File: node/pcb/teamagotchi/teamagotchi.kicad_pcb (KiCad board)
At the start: 2 copper layers, 75 x 112 mm, 24 parts, among them M1 Motor_DC, Q1 BC547, SW1 SW_Push, SW2 SW_Push, SW3 SW_Push, SW4 SW_Push, SW5 SW_Push, U1 3406

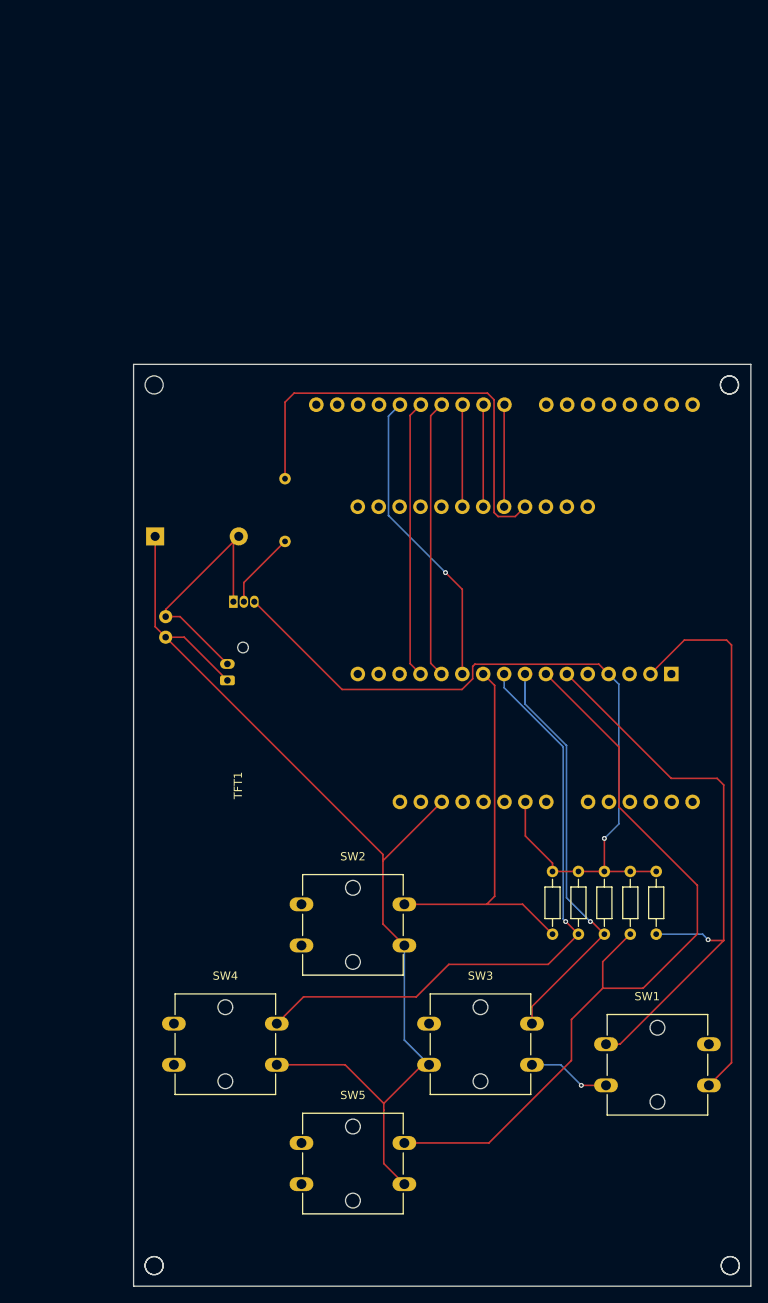
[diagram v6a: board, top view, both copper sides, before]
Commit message: added GND copper filling, added RIOT and HAW Logo
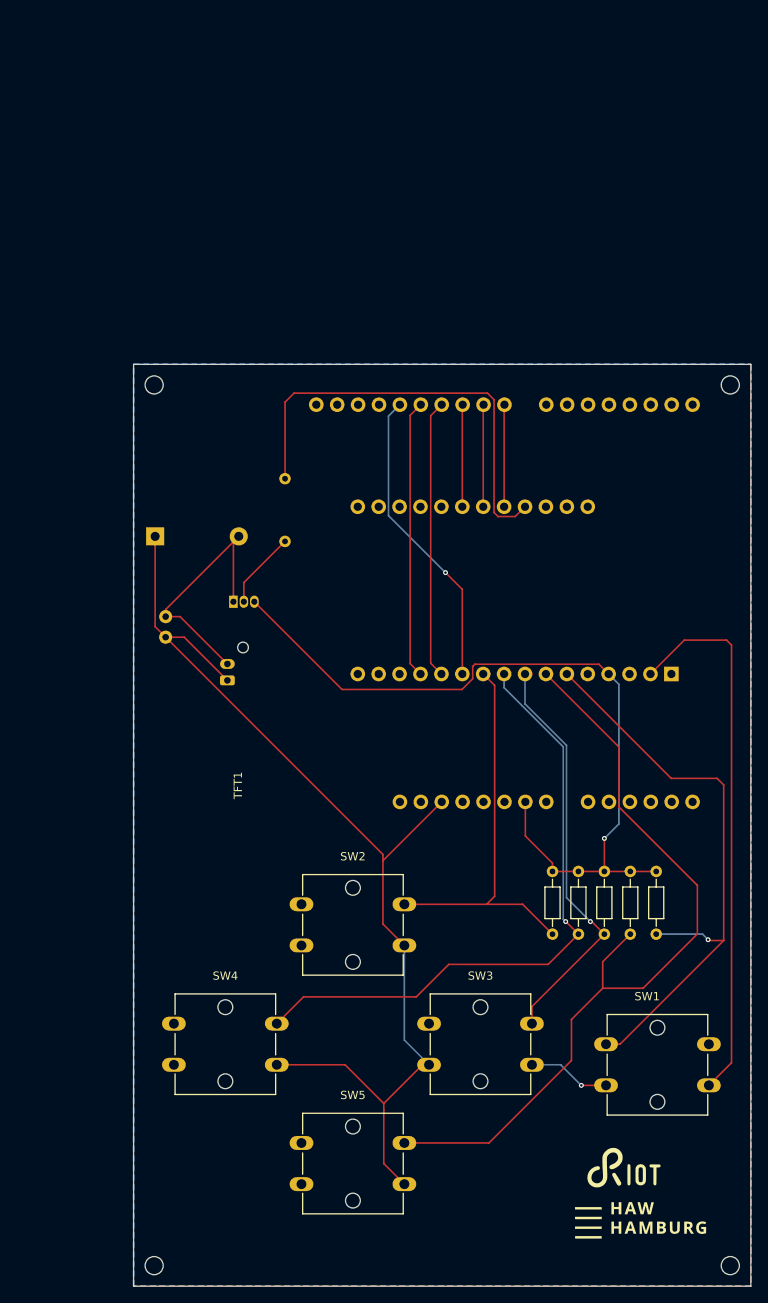
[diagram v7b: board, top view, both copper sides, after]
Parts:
- removed ? (x3): , 
- added G***: LOGO, Library:haw_logo_logo, F.Cu at (171.0, 150.7)
- added G***: LOGO, Library:riot_logo, F.Cu at (169.6, 144.3)
- moved REF** 0.10 mm to (182.5, 49.2)
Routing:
- added copper zone on B.Cu, net Net-(D1-K)
- added copper zone on F.Cu, net Net-(D1-K)

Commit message: added debouncing, some beautyfications
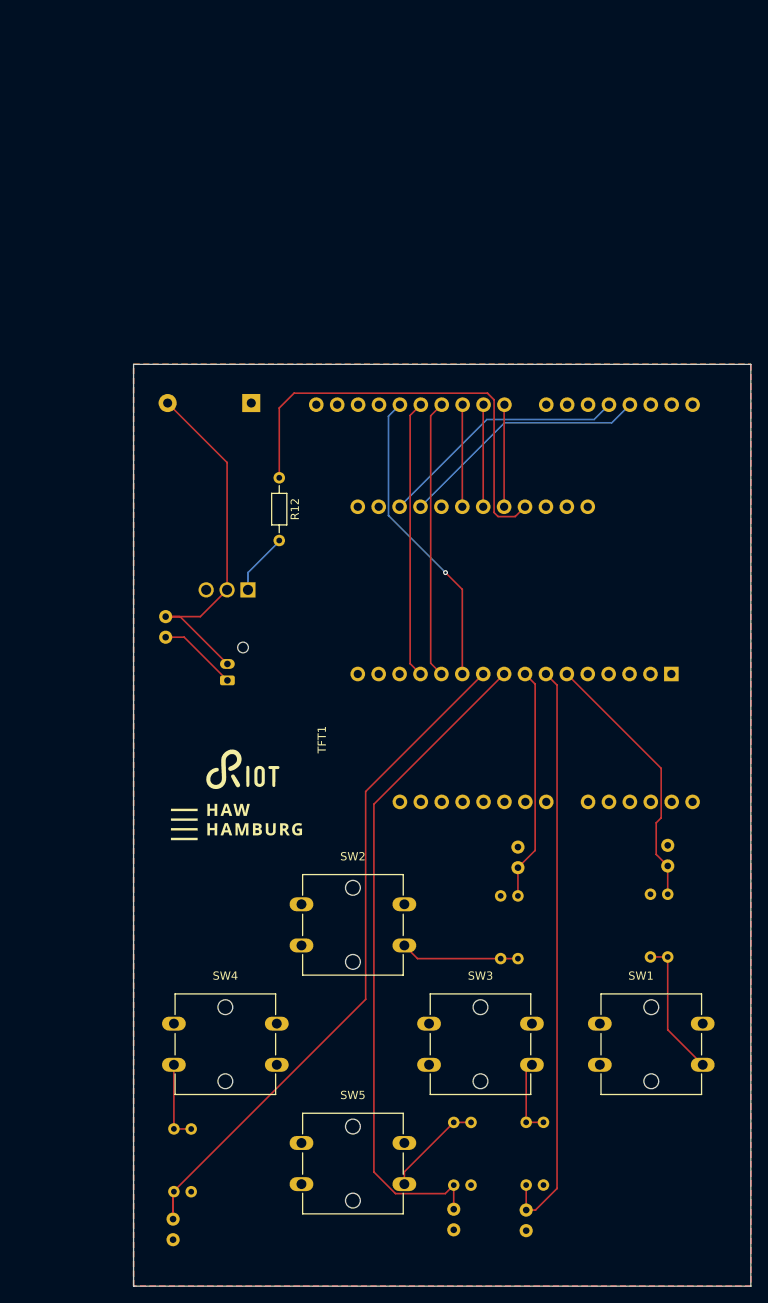
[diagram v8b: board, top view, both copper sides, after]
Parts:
- removed Q1: BC547, Package_TO_SOT_THT:TO-92_Inline
- removed REF** (x4): 2.2mm_M2, MountingHole:MountingHole_2.2mm_M2
- added C2: C, Capacitor_THT:C_Disc_D3.0mm_W1.6mm_P2.50mm, B.Cu at (174.9, 107.6)
- added C3: C, Capacitor_THT:C_Disc_D3.0mm_W1.6mm_P2.50mm, B.Cu at (156.7, 107.9)
- added C4: C, Capacitor_THT:C_Disc_D3.0mm_W1.6mm_P2.50mm, B.Cu at (157.7, 149.5)
- added C5: C, Capacitor_THT:C_Disc_D3.0mm_W1.6mm_P2.50mm, B.Cu at (114.8, 150.6)
- added C6: C, Capacitor_THT:C_Disc_D3.0mm_W1.6mm_P2.50mm, B.Cu at (148.9, 149.4)
- added Q2: IRLZ44N, Library:IRLZ44N, B.Cu at (121.3, 73.2)
- added R10: R, Resistor_THT:R_Axial_DIN0204_L3.6mm_D1.6mm_P7.62mm_Horizontal, B.Cu at (151.0, 146.4)
- added R12: R, Resistor_THT:R_Axial_DIN0204_L3.6mm_D1.6mm_P7.62mm_Horizontal, F.Cu at (127.7, 60.5)
- added R7: R, Resistor_THT:R_Axial_DIN0204_L3.6mm_D1.6mm_P7.62mm_Horizontal, B.Cu at (114.9, 147.2)
- added R8: R, Resistor_THT:R_Axial_DIN0204_L3.6mm_D1.6mm_P7.62mm_Horizontal, B.Cu at (117.0, 147.2)
- added R9: R, Resistor_THT:R_Axial_DIN0204_L3.6mm_D1.6mm_P7.62mm_Horizontal, B.Cu at (148.9, 146.4)
- R1, R2, R3, R4, R5: moved to B.Cu
- moved R6 91.4 mm to (159.8, 146.4), turned to 90 degrees
- moved G*** 68.9 mm to (121.9, 102.3)
- moved G*** 67.0 mm to (123.3, 95.9)
- moved R5 38.2 mm to (157.7, 146.4), turned to 90 degrees
- moved D1 20.0 mm to (124.3, 51.4), turned to 180 degrees
- moved R3 10.9 mm to (156.7, 111.3)
- moved R4 9.91 mm to (154.6, 111.3)
- moved R2 3.70 mm to (172.8, 111.1)
- moved R1 3.10 mm to (174.9, 111.1)
- moved SW1 2.61 mm to (166.6, 126.8)
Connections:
- net Net-(TFT1-D10/TFT_CS) renamed /TFT_CS
- net Net-(TFT1-D11/MOSI) renamed /MOSI
- net Net-(TFT1-D12/MISO) renamed /MISO
- net Net-(TFT1-D13/SCLK) renamed /SCK
- net Net-(TFT1-D8/Touch_CS) renamed /TOUCH_CS
- net Net-(TFT1-D9/TFT_DC) renamed /TFT_DC
- C1 pad 1: Net-(D1-K) -> /3.3V
- D1 pad 1: Net-(D1-K) -> /3.3V
- M1 pad 1: Net-(D1-K) -> /3.3V
- R1 pad 1: Net-(Q1-E) -> /SW1
- R1 pad 2: Net-(U1-A1/0.03) -> Net-(R1-Pad2)
- R2 pad 1: Net-(Q1-E) -> /3.3V
- R2 pad 2: Net-(U1-A2/0.04) -> Net-(R1-Pad2)
- R3 pad 1: Net-(Q1-E) -> /SW2
- R3 pad 2: Net-(U1-A3/0.05) -> Net-(R3-Pad2)
- R4 pad 1: Net-(Q1-E) -> /3.3V
- R4 pad 2: Net-(U1-A4/0.28) -> Net-(R3-Pad2)
- R5 pad 1: Net-(Q1-E) -> /SW3
- R5 pad 2: Net-(U1-A5/0.29) -> Net-(R5-Pad2)
- R6 pad 1: Net-(U1-P0.16) -> /3.3V
- R6 pad 2: Net-(Q1-B) -> Net-(R5-Pad2)
- SW1 pad 1: Net-(U1-A1/0.03) -> /GND
- SW1 pad 2: Net-(D1-K) -> Net-(R1-Pad2)
- SW2 pad 1: Net-(U1-A5/0.29) -> /GND
- SW2 pad 2: Net-(D1-K) -> Net-(R3-Pad2)
- SW3 pad 1: Net-(U1-A3/0.05) -> /GND
- SW3 pad 2: Net-(D1-K) -> Net-(R5-Pad2)
- SW4 pad 1: Net-(U1-A4/0.28) -> /GND
- SW4 pad 2: Net-(D1-K) -> Net-(R7-Pad2)
- SW5 pad 1: Net-(U1-A2/0.04) -> /GND
- SW5 pad 2: Net-(D1-K) -> Net-(R10-Pad2)
- TFT1 pad 3: (no net) -> /BACK_LITE
- TFT1 pad 4: unconnected-(TFT1-D4/SD_CS-Pad4) -> /SD_CS
- TFT1 pad 40: Net-(Q1-E) -> /GND
- TFT1 pad 50: Net-(D1-K) -> /3.3V
- U1 pad 10: Net-(U1-A5/0.29) -> /SW4
- U1 pad 19: unconnected-(U1-P0.27-Pad19) -> /SD_CS
- U1 pad 2: Net-(D1-K) -> /3.3V
- U1 pad 20: unconnected-(U1-A6/P0.30-Pad20) -> /BACK_LITE
- U1 pad 25: Net-(U1-P0.16) -> /VIB_MOTOR
- U1 pad 3: Net-(D1-K) -> /3.3V
- U1 pad 4: Net-(Q1-E) -> /GND
- U1 pad 6: Net-(U1-A1/0.03) -> /SW1
- U1 pad 7: Net-(U1-A2/0.04) -> /SW3
- U1 pad 8: Net-(U1-A3/0.05) -> /SW2
- U1 pad 9: Net-(U1-A4/0.28) -> /SW5
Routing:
- net Net-(D1-K): track 208.1 -> 0.00 mm, vias 1 -> 0
- net Net-(Q1-E): track 97.8 -> 0.00 mm, vias 1 -> 0
- net Net-(U1-A2/0.04): track 97.1 -> 0.00 mm
- net /SW4: track 0.00 -> 85.2 mm
- net /SW5: track 0.00 -> 81.2 mm
- net Net-(U1-A4/0.28): track 76.5 -> 0.00 mm, vias 1 -> 0
- net Net-(U1-A1/0.03): track 71.9 -> 0.00 mm, vias 1 -> 0
- net /SW3: track 0.00 -> 70.9 mm
- net /VIB_MOTOR: track 0.00 -> 53.8 mm
- net Net-(U1-P0.16): track 53.6 -> 0.00 mm
- net Net-(U1-A3/0.05): track 51.1 -> 0.00 mm, vias 1 -> 0
- net Net-(U1-A5/0.29): track 48.5 -> 0.00 mm
- net /SW1: track 0.00 -> 32.6 mm
- net /BACK_LITE: track 0.00 -> 30.6 mm
- net /SD_CS: track 0.00 -> 30.6 mm
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- added copper zone on F.Cu, net /3.3V
- added copper zone on B.Cu, net /GND
- removed copper zone on B.Cu, net Net-(D1-K)
- removed copper zone on F.Cu, net Net-(D1-K)
